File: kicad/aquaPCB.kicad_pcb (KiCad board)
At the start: 2 copper layers, 100 x 100 mm, 149 parts, among them J1 12V IN, J11 SSR G17, J12 SSR G22, J13 SSR G23, J14 SSR G27, J15 IN1, J16 IN2, J17 IN3, J18 IN4, J19 1-Wire 1, J2 Raspberry Pi, J22 I2C 1, J23 I2C 2, J24 Display, J25 pH probe, J26 Module, J27 AIN3, J4 OUT G18, J5 OUT G19, J6 OUT G12, J7 OUT G13, J8 OUT G16, J9 OUT G26, Q1 AOD4184A, Q10 AOD4185, Q2 AOD4184A, Q3 AOD4184A, Q4 AOD4184A, Q5 AOD4184A, Q6 AOD4184A, U1 TPS54360B, U2 AMS1117-3.3, U3 74HCT244D, U4 ULN2803A, U5 ADS1115IDGSR, U6 TLV9062IDR

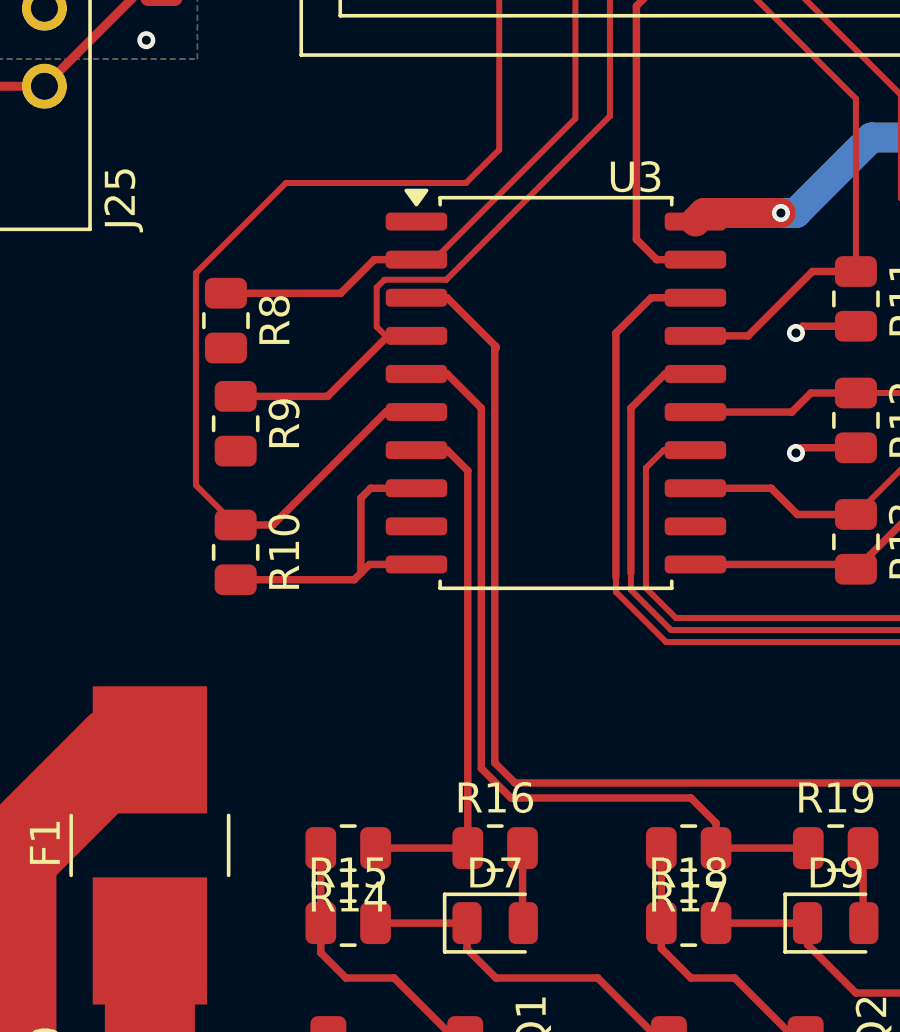
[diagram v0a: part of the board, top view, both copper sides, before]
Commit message: kicad: routing progress (by hand)
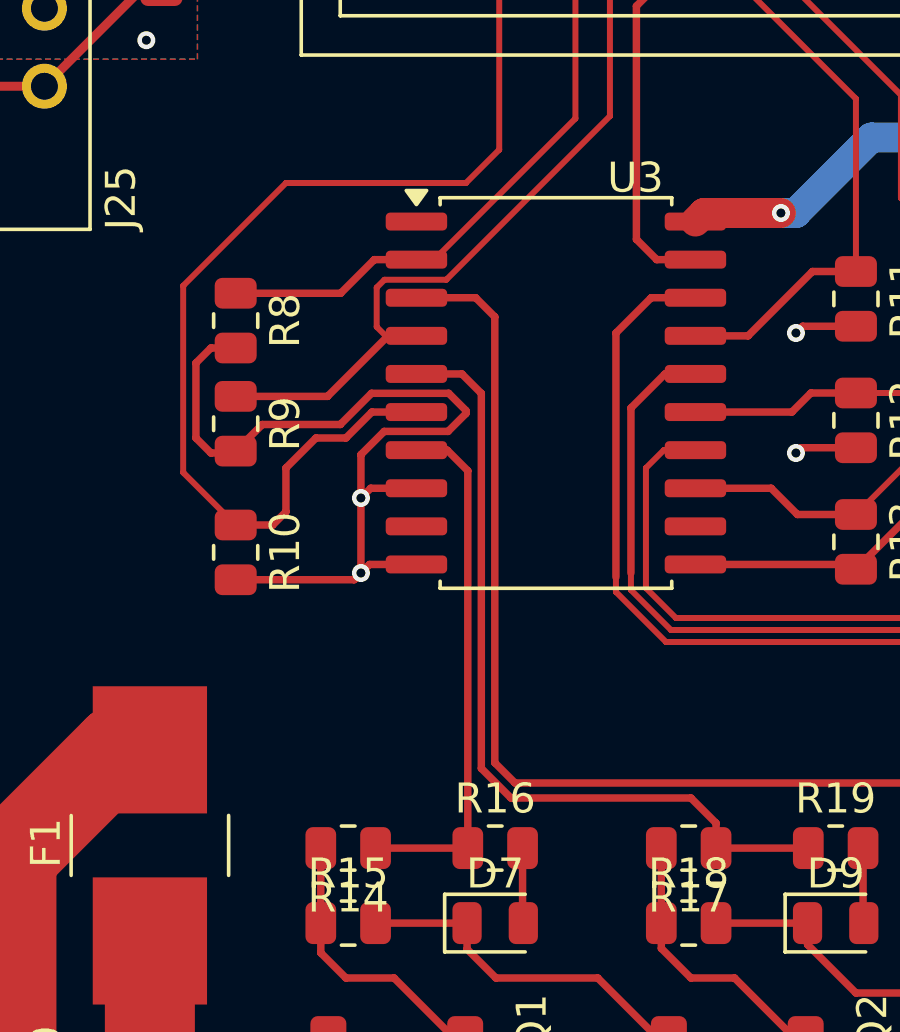
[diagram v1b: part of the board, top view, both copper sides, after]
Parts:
- moved R8 0.33 mm to (97.3, 88.6)
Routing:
- net GND: track 415.9 -> 435.5 mm, vias 41 -> 43
- net GPIO26_Q6: track 37.8 -> 39.0 mm
- net /Power outputs Q1..Q6/Q3_DRV: track 40.8 -> 41.3 mm

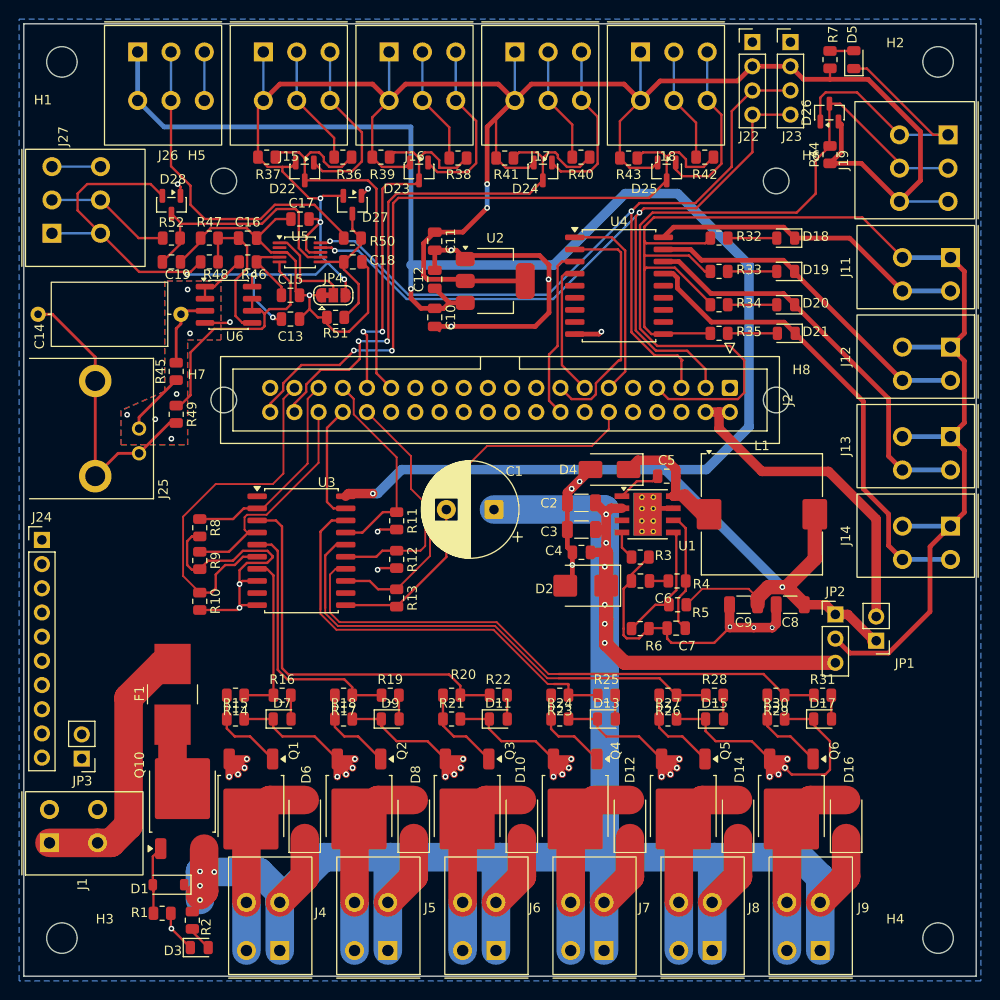
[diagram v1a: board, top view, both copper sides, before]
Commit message: kicad: routing progress (by hand)
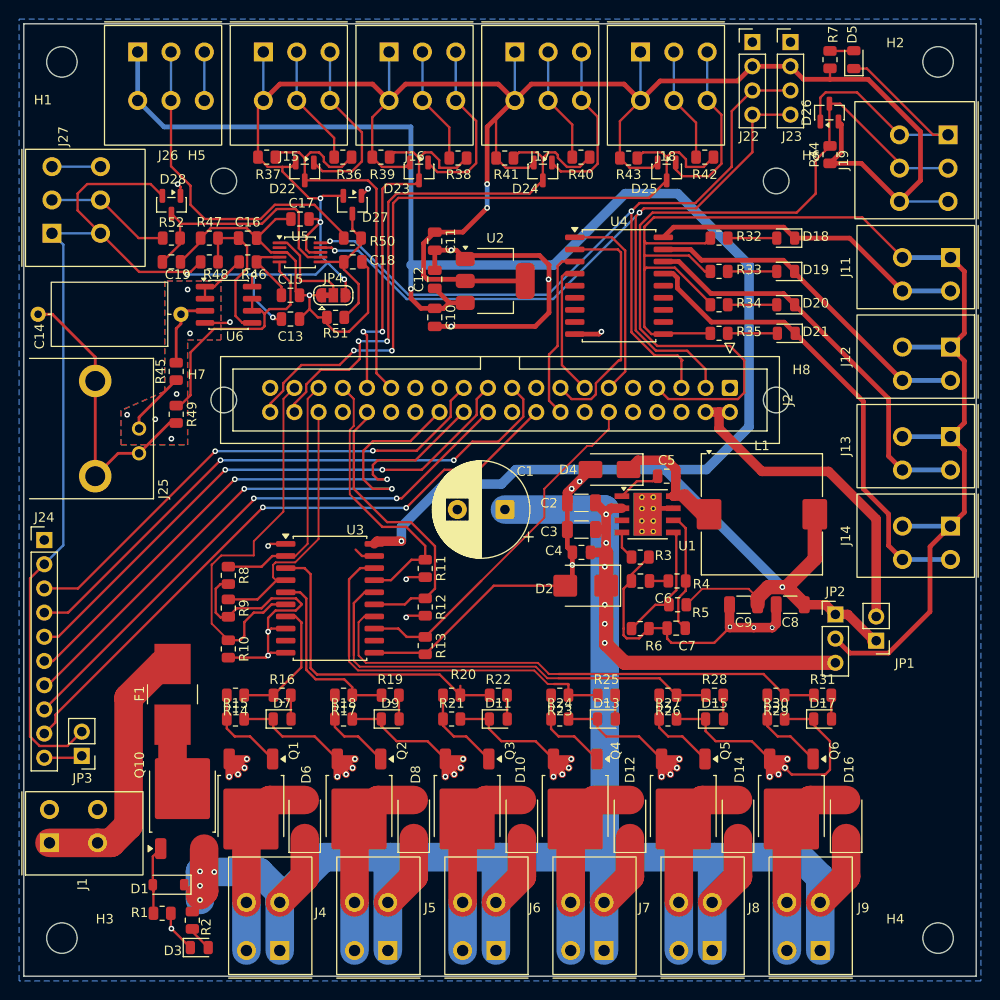
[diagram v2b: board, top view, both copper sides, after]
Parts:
- moved R10 5.83 mm to (100.3, 101.3)
- moved R11 5.83 mm to (121.0, 92.9)
- moved R12 5.83 mm to (121.0, 96.9)
- moved R13 5.83 mm to (121.0, 101.0)
- moved R8 5.83 mm to (100.3, 93.6)
- moved R9 5.83 mm to (100.3, 97.0)
- moved U3 5.83 mm to (111.0, 96.0)
- moved C1 1.15 mm to (129.4, 86.7)
- moved JP3 0.28 mm to (84.9, 112.5)
- moved J24 0.25 mm to (81.0, 89.9)
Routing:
- net GPIO24_DISP_RST: track 0.00 -> 66.2 mm, vias 0 -> 2
- net GPIO10_MOSI: track 0.00 -> 62.3 mm, vias 0 -> 2
- net GPIO7_CE1: track 0.00 -> 61.8 mm, vias 0 -> 2
- net +3V3: track 288.5 -> 349.7 mm
- net GPIO25_DISP_DC: track 0.00 -> 59.6 mm, vias 0 -> 2
- net GPIO8_CE0: track 0.00 -> 58.5 mm, vias 0 -> 2
- net GPIO9_MISO: track 0.00 -> 58.4 mm, vias 0 -> 2
- net GPIO11_SCLK: track 0.00 -> 53.8 mm, vias 0 -> 2
- net GPIO13_Q3: track 23.3 -> 31.3 mm
- net /Power outputs Q1..Q6/Q2_DRV: track 27.4 -> 19.4 mm
- net /Power outputs Q1..Q6/Q3_DRV: track 41.3 -> 33.7 mm
- net GPIO12_Q2: track 25.4 -> 31.2 mm
- net /Power outputs Q1..Q6/Q6_DRV: track 60.3 -> 55.0 mm
- net /Power outputs Q1..Q6/Q4_DRV: track 45.1 -> 40.0 mm
- net /Power outputs Q1..Q6/Q5_DRV: track 52.2 -> 47.1 mm
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
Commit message: kicad: move C1, routing improvements (by hand)
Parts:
- moved C1 13.0 mm to (131.5, 99.5)
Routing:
- net VIN: track 269.6 -> 342.1 mm
- net /Power supply/VIN_RAW: track 28.5 -> 49.0 mm, vias 0 -> 6
- net GND: track 431.9 -> 441.3 mm, vias 44 -> 68
- net +5V: track 216.4 -> 214.0 mm, vias 3 -> 6
